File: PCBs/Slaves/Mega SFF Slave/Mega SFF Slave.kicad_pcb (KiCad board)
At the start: 2 copper layers, 87.1 x 57 mm, 80 parts, among them J1 AVR-ISP-6, J10 Screw_Terminal_01x02, J11 Screw_Terminal_01x02, J12 Screw_Terminal_01x02, J13 Screw_Terminal_01x02, J14 Screw_Terminal_01x02, J15 Screw_Terminal_01x02, J16 Screw_Terminal_01x02, J17 Screw_Terminal_01x02, J18 Screw_Terminal_01x02, J19 Screw_Terminal_01x02, J2 Screw_Terminal_01x02, J20 Screw_Terminal_01x02, J21 Screw_Terminal_01x02, J22 Screw_Terminal_01x02, J23 Screw_Terminal_01x02, J24 Screw_Terminal_01x02, J25 Screw_Terminal_01x02, J26 Screw_Terminal_01x02, J27 Screw_Terminal_01x02, J28 Screw_Terminal_01x02, J29 Screw_Terminal_01x02, J3 Screw_Terminal_01x02, J30 Screw_Terminal_01x02, J31 Screw_Terminal_01x02, J32 Screw_Terminal_01x02, J33 Screw_Terminal_01x02, J34 Screw_Terminal_01x02, J35 Screw_Terminal_01x02, J36 Screw_Terminal_01x02, J37 Screw_Terminal_01x02, J39 Conn_01x06_Female, J4 Screw_Terminal_01x02, J40 Screw_Terminal_01x02, J41 Screw_Terminal_01x02, J5 Screw_Terminal_01x02, J6 Screw_Terminal_01x02, J7 Screw_Terminal_01x02, J8 Screw_Terminal_01x02, J9 Screw_Terminal_01x02, SW1 SW_MEC_5E, SW2 SW_DIP_x02, SW3 SW_DIP_x02, U1 ATmega2560-16A, U2 MAX487ESA+T, U3 AMS1117-5.0, U4 ULN2003A, U5 MAX487ESA+T, Y1 Crystal_GND24

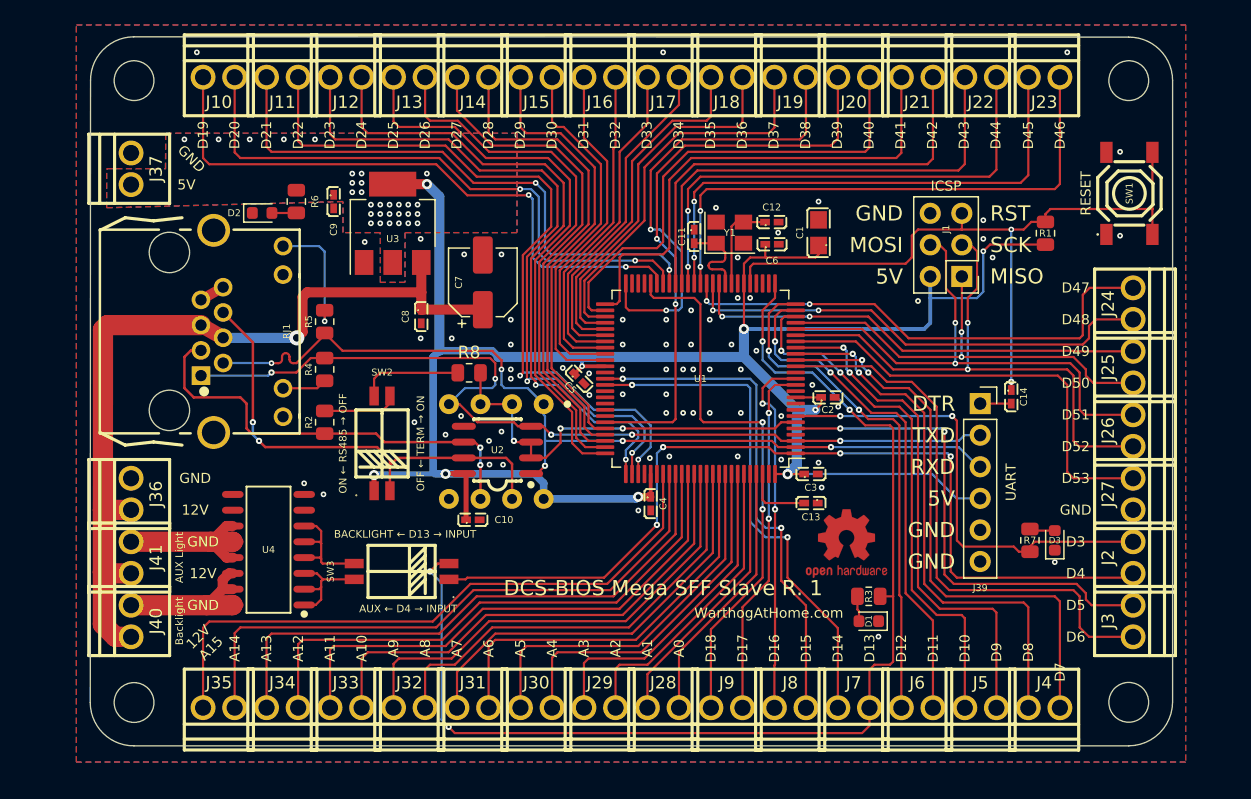
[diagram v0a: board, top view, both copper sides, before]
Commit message: Updated Mega SFF Slave RS485 Switch and Silkscreen
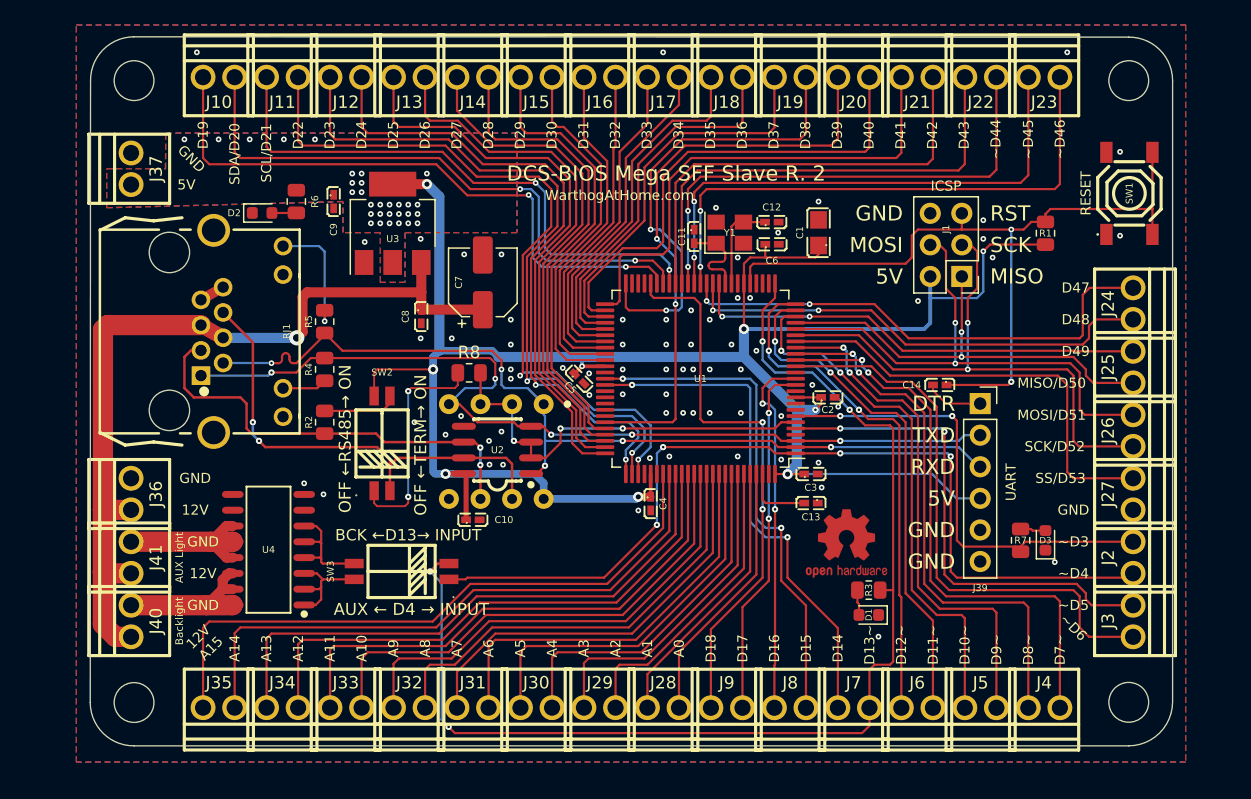
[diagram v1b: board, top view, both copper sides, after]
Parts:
- moved C14 5.83 mm to (149.8, 94.5), turned to 180 degrees
- moved D3 0.75 mm to (158.3, 107.0)
- moved R7 0.75 mm to (156.3, 107.0)
- moved D1 0.50 mm to (144.1, 113.0)
- moved R3 0.50 mm to (144.1, 111.0)
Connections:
- SW2 pad 1: +5V -> Net-(R8-Pad1)
- SW2 pad 4: Net-(R8-Pad1) -> +5V
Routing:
- net Net-(R8-Pad1): track 8.32 -> 18.1 mm, vias 0 -> 2
- net RESET: track 57.8 -> 62.5 mm
- net FTDI_DTR: track 2.50 -> 4.68 mm
- net +5V: track 169.7 -> 170.2 mm
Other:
- board text added: "BCK ←D13→ INPUT"
- board text added: "OFF ←RS485→ ON"
- board text added: "OFF ←TERM→ ON"
- board text removed: "BACKLIGHT ← D13 → INPUT"
- board text removed: "OFF ← TERM → ON"
- board text removed: "ON ← RS485 → OFF"

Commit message: Added Hotplug and RS485 protection to Mega SFF. Capacitor LCSC numbers to go.
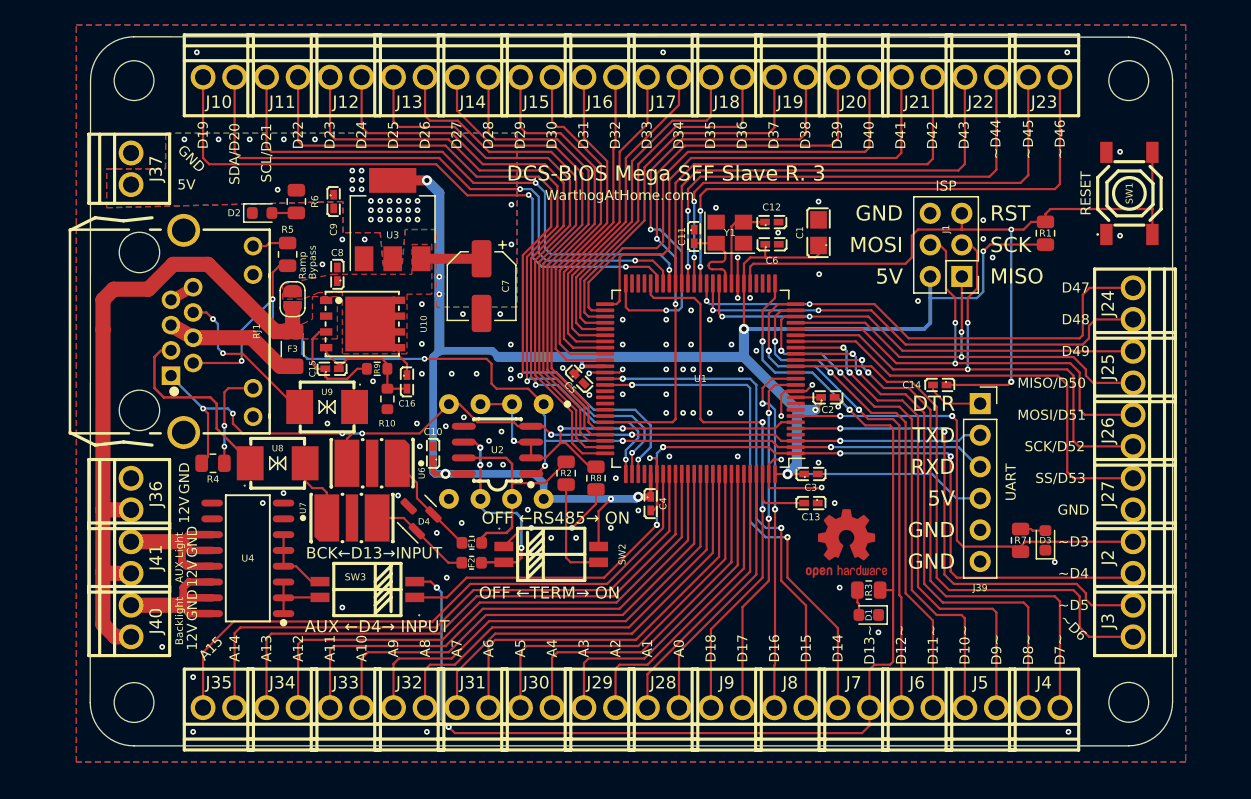
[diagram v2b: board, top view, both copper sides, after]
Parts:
- added C15: 500nF, A10 KiCad Libraries:C0402, F.Cu at (100.9, 93.2)
- added C16: 50nF, A10 KiCad Libraries:C0402, F.Cu at (107.0, 94.2)
- added D4: SM712_SOT23, Package_TO_SOT_SMD:SOT-23, F.Cu at (107.8, 104.9)
- added F1: 100mA, Fuse:Fuse_0603_1608Metric, F.Cu at (112.2, 107.2)
- added F2: 100mA, Fuse:Fuse_0603_1608Metric, F.Cu at (112.2, 108.8)
- added F3: 500mA, Fuse:Fuse_1206_3216Metric, F.Cu at (97.8, 91.6)
- added JP1: Solder, Jumper:SolderJumper-2_P1.3mm_Open_RoundedPad1.0x1.5mm, F.Cu at (97.8, 87.6)
- added R10: 1M, Resistor_SMD:R_0603_1608Metric, F.Cu at (105.4, 95.6)
- added R9: 10M, Resistor_SMD:R_0603_1608Metric, F.Cu at (104.6, 93.2)
- added U10: HY15P03C2, A10 KiCad Libraries:DFN-8_L5.9-W5.2-P1.27-LS6.2-BL, F.Cu at (103.4, 89.6)
- added U6: TBU-CA065-200-WH, A10 KiCad Libraries:DIO-SMD_3P-L6.5-W4.0-BI, F.Cu at (104.2, 100.8)
- added U7: TBU-CA065-200-WH, A10 KiCad Libraries:DIO-SMD_3P-L6.5-W4.0-BI, F.Cu at (102.5, 105.2)
- added U8: TISP4240M3BJR-S, A10 KiCad Libraries:DO-214AA_L4.4-W3.6-LS5.3-BI, F.Cu at (96.6, 100.8)
- added U9: TISP4240M3BJR-S, A10 KiCad Libraries:DO-214AA_L4.4-W3.6-LS5.3-BI, F.Cu at (100.5, 96.2)
- moved R2 19.8 mm to (119.8, 101.6), turned to -90 degrees
- moved SW2 16.3 mm to (118.6, 108.1), turned to -90 degrees
- moved R8 13.3 mm to (122.2, 102.0), turned to 90 degrees
- moved R4 11.7 mm to (91.4, 100.8), turned to 180 degrees
- moved C8 7.56 mm to (101.4, 85.6), turned to 90 degrees
- moved C10 6.23 mm to (109.1, 100.0), turned to 90 degrees
- moved R5 6.17 mm to (97.4, 84.0)
- moved SW3 3.11 mm to (103.8, 110.9)
- moved RJ1 2.41 mm to (87.9, 90.2)
- moved U4 1.80 mm to (94.2, 108.4)
- moved C7 0.32 mm to (113.0, 86.5), turned to -90 degrees
- moved U3 0.30 mm to (105.8, 81.2)
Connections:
- C7 pad 1: +12V -> 12V_Ramped
- C8 pad 1: +12V -> 12V_Ramped
- J36 pad 1: +12V -> 12V_Fused
- J40 pad 1: +12V -> 12V_Fused
- J41 pad 1: +12V -> 12V_Fused
- R2 pad 1: RS485+ -> TERM_B
- SW2 pad 2: RS485- -> TERM_A
- U2 pad 6: RS485+ -> TERM_A
- U2 pad 7: RS485- -> TERM_B
- U3 pad 3: +12V -> 12V_Ramped
- U5 pad 6: RS485+ -> TERM_A
- U5 pad 7: RS485- -> TERM_B
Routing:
- net 12V_Fused: track 0.00 -> 62.7 mm
- net +12V: track 68.9 -> 11.0 mm, vias 1 -> 0
- net RS485-: track 38.3 -> 12.9 mm
- net GND: track 2.05 -> 25.0 mm, vias 71 -> 95
- net RS485+: track 35.1 -> 14.7 mm, vias 2 -> 0
- net TERM_B: track 0.00 -> 17.5 mm
- net TERM_A: track 0.00 -> 16.5 mm, vias 0 -> 3
- net RXD: track 73.7 -> 84.1 mm, vias 5 -> 6
- net Net-(C15-Pad2): track 0.00 -> 10.2 mm
- net Net-(D4-Pad2): track 0.00 -> 8.57 mm
- net Net-(D4-Pad1): track 0.00 -> 8.30 mm
- net Net-(R8-Pad1): track 18.1 -> 9.99 mm
- net 12V_Ramped: track 0.00 -> 7.32 mm
- net Net-(R5-Pad1): track 10.0 -> 2.88 mm, vias 1 -> 0
- net Net-(U7-Pad1): track 0.00 -> 5.59 mm
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- added copper zone on F.Cu, net 12V_Fused
- added copper zone on F.Cu, net 12V_Ramped
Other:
- board text added: "AUX ←D4→ INPUT"
- board text added: "BCK←D13→INPUT"
- board text removed: "AUX ← D4 → INPUT"
- board text removed: "BCK ←D13→ INPUT"

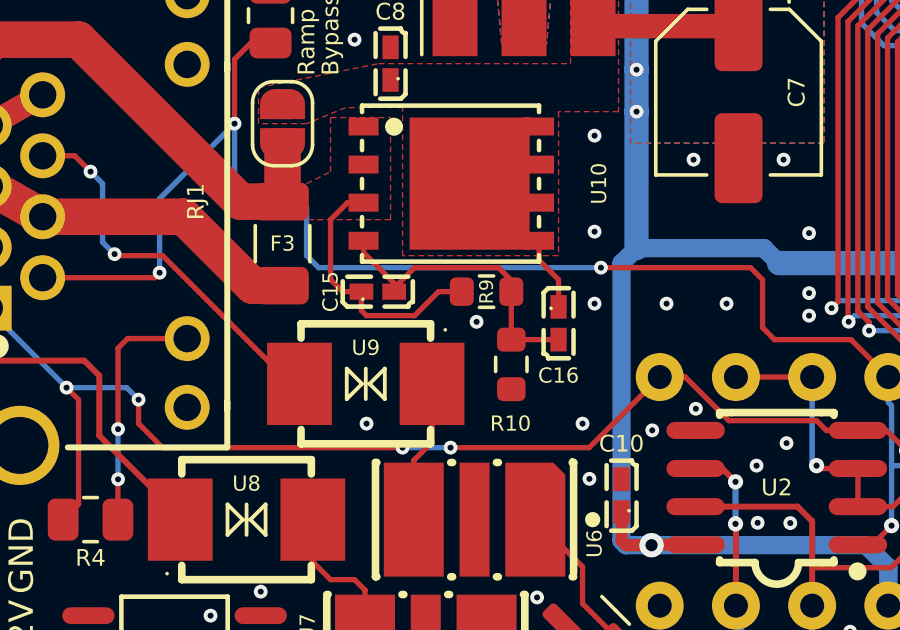
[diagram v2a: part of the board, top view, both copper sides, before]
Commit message: Updated LCSC number and size of voltage ramp capacitors for Mega SFF Slave
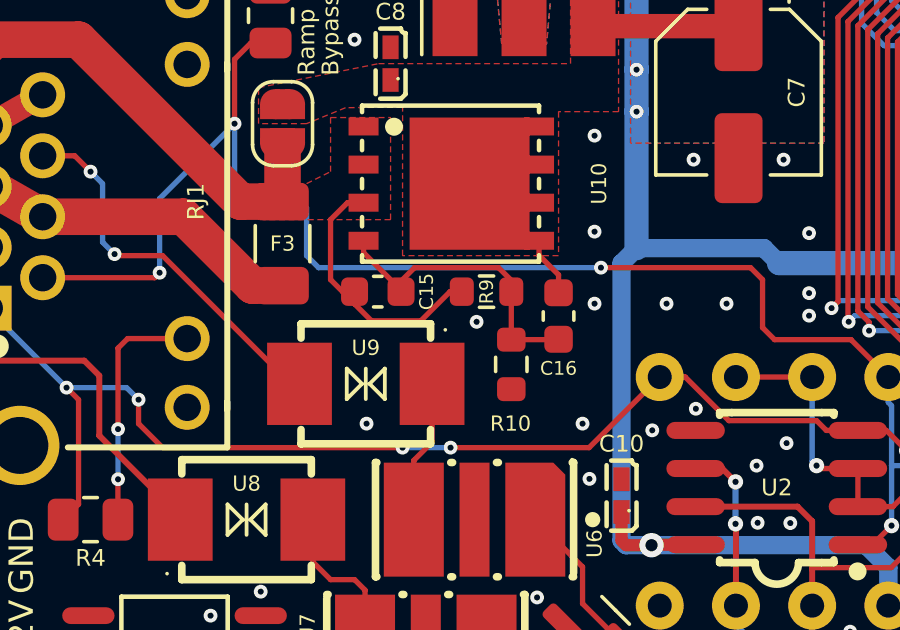
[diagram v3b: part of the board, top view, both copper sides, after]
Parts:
- C15: value 500nF -> 470nF; footprint A10 KiCad Libraries:C0402 -> Capacitor_SMD:C_0603_1608Metric
- C16: value 50nF -> 47nF; footprint A10 KiCad Libraries:C0402 -> Capacitor_SMD:C_0603_1608Metric
- moved C16 0.24 mm to (107.0, 94.0)

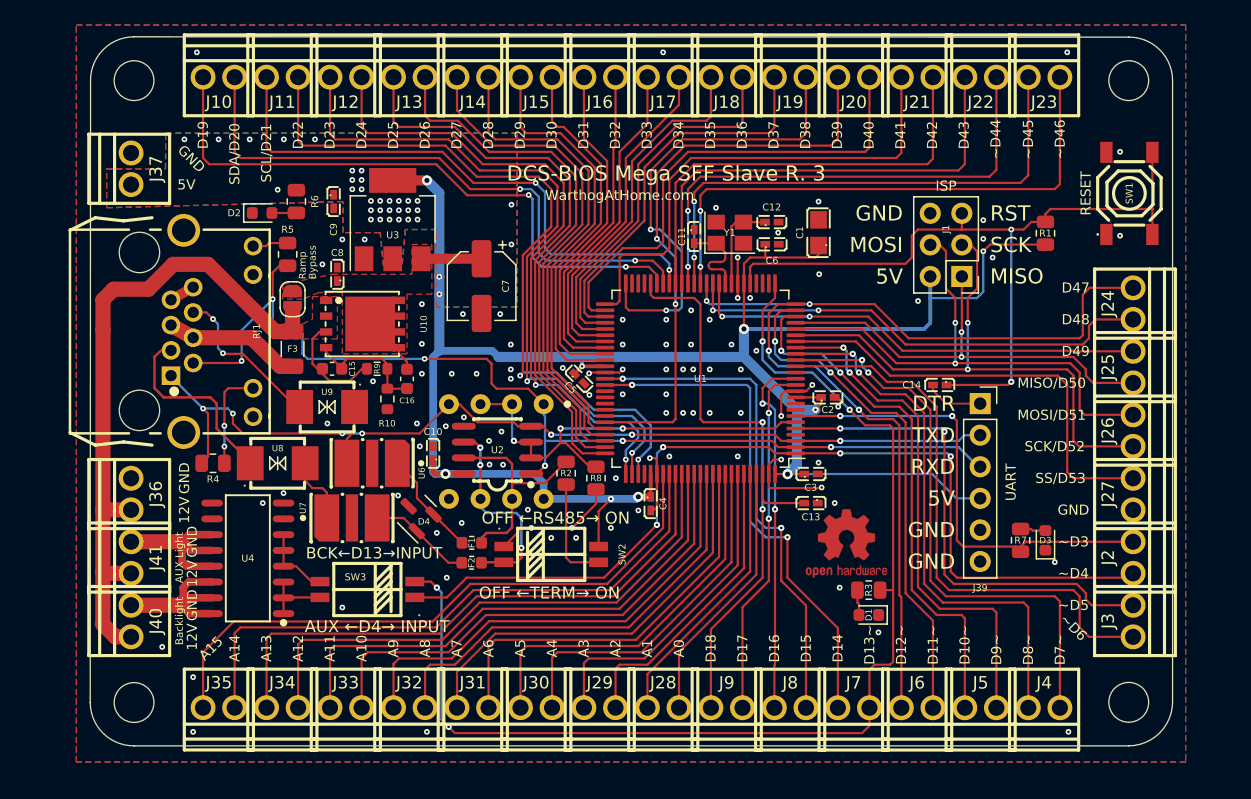
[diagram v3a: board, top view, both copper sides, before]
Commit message: Updated Mega SFF Slave for correct terminal block size
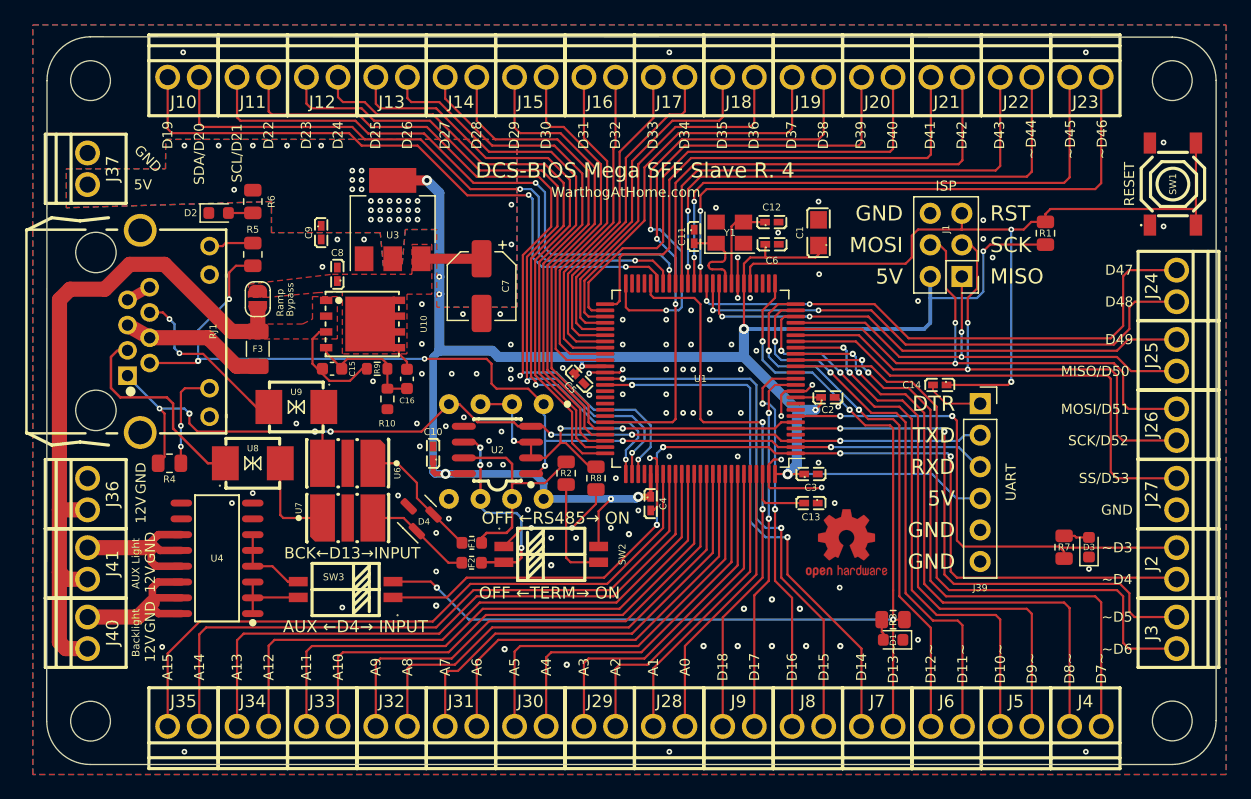
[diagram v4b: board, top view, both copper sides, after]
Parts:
- moved H3 3.81 mm to (81.5, 121.5)
- moved H4 3.81 mm to (168.5, 121.5)
- moved J24 3.78 mm to (169.0, 86.5)
- moved J4 3.65 mm to (161.5, 122.1)
- moved J25 3.63 mm to (169.0, 92.1)
- moved J3 3.63 mm to (169.0, 114.4)
- moved J40 3.63 mm to (81.1, 114.4)
- moved SW1 3.58 mm to (168.6, 78.3)
- moved D3 3.54 mm to (161.8, 107.5)
- moved R7 3.54 mm to (159.8, 107.5)
- moved J2 3.53 mm to (169.0, 108.8)
- moved J41 3.53 mm to (81.1, 108.8)
- moved J26 3.53 mm to (169.0, 97.7)
- moved D2 3.50 mm to (91.8, 80.6)
- moved H1 3.50 mm to (81.5, 70.0)
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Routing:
- net D13: track 93.7 -> 85.8 mm
- net D4: track 76.1 -> 81.2 mm
- net D7: track 46.2 -> 51.0 mm
- net D8: track 43.9 -> 48.6 mm
- net D6: track 45.7 -> 50.3 mm
- net D48: track 38.5 -> 43.1 mm
- net D47: track 40.5 -> 45.1 mm
- net D5: track 40.1 -> 44.5 mm
- net A15: track 49.9 -> 54.2 mm
- net D10: track 42.7 -> 47.0 mm
- net A14: track 48.9 -> 53.2 mm
- net D9: track 41.6 -> 45.8 mm
- net D49: track 37.0 -> 40.8 mm
- net D3: track 37.9 -> 41.7 mm
- net A12: track 44.6 -> 48.4 mm
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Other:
- board size 87.1 x 57 mm -> 94.1 x 58.5 mm
- board text added: "51.5MM"
- board text added: "87MM"
- board text removed: "50MM"
- board text removed: "80MM"
